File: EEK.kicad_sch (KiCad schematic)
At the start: 34 parts

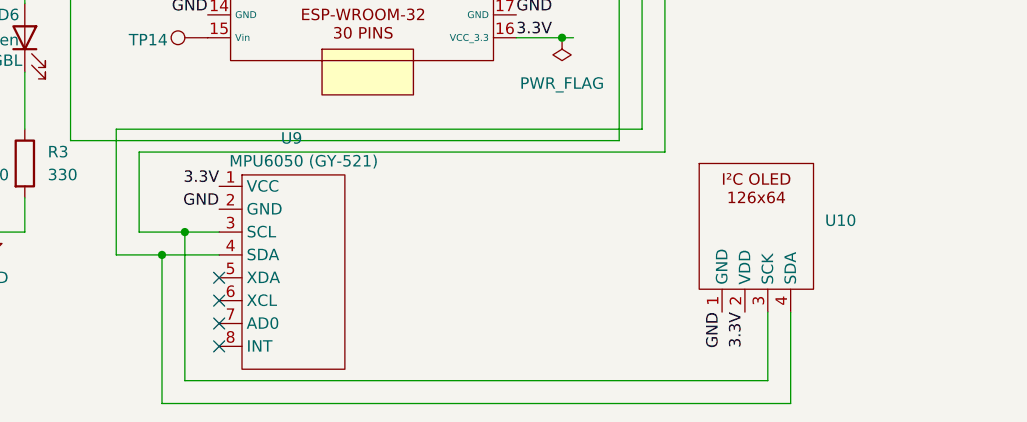
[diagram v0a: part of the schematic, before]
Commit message: fix the bug on OLED power supply pin1 and 2 inverted (3.3V and GND)
Fix the bug on the OLED power supply pins which have been inverted PIN 1 3.3V and pin 2 GND
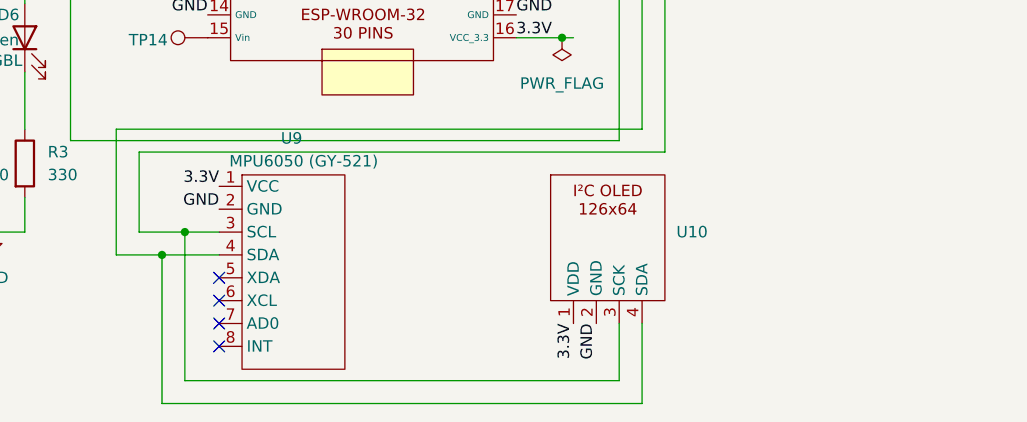
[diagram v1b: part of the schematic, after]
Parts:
- U10: footprint Connector_PinHeader_2.54mm:PinHeader_1x04_P2.54mm_Vertical -> (none)
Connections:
- net 3.3V: now also U10.1 (VDD); no longer U10.2 (VDD)
- net GND: now also U10.2 (GND); no longer U10.1 (GND)
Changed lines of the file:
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@@
+	(wire
+		(pts
+			(xy 127 124.46) (xy 73.66 124.46)
+		)
+		(stroke
+			(width 0)
+			(type default)
+		)
+	)
 	(wire
 		(pts
@@
 	(wire
 		(pts
+			(xy 124.46 121.92) (xy 76.2 121.92)
+		)
+		(stroke
+			(width 0)
+			(type default)
+		)
+	)
+	(wire
+		(pts
 			(xy 127 58.42) (xy 127 93.98)
 		)
@@
 	(wire
 		(pts
-			(xy 143.51 124.46) (xy 73.66 124.46)
-		)
-		(stroke
-			(width 0)
-			(type default)
-		)
-	)
-	(wire
-		(pts
 			(xy 73.66 107.95) (xy 80.01 107.95)
 		)
@@
 	(wire
 		(pts
-			(xy 140.97 114.3) (xy 140.97 121.92)
-		)
-		(stroke
-			(width 0)
-			(type default)
-		)
-	)
-	(wire
-		(pts
 			(xy 66.04 43.18) (xy 41.91 43.18)
 		)
@@
 	(wire
 		(pts
+			(xy 124.46 115.57) (xy 124.46 121.92)
+		)
+		(stroke
+			(width 0)
+			(type default)
+		)
+	)
+	(wire
+		(pts
 			(xy 60.96 68.58) (xy 78.74 68.58)
 		)
@@
 	(wire
 		(pts
-			(xy 143.51 114.3) (xy 143.51 124.46)
-		)
-		(stroke
-			(width 0)
-			(type default)
-		)
-	)
-	(wire
-		(pts
 			(xy 41.91 64.77) (xy 49.53 64.77)
 		)
@@
 	(wire
 		(pts
-			(xy 140.97 121.92) (xy 76.2 121.92)
-		)
-		(stroke
-			(width 0)
-			(type default)
-		)
-	)
-	(wire
-		(pts
 			(xy 68.58 71.12) (xy 78.74 71.12)
 		)
@@
 		(pts
 			(xy 77.47 60.96) (xy 78.74 60.96)
+		)
+		(stroke
+			(width 0)
+			(type default)
+		)
+	)
+	(wire
+		(pts
+			(xy 127 115.57) (xy 127 124.46)
 		)
 		(stroke
@@
 	)
 	(label "3.3V"
-		(at 138.43 114.3 270)
+		(at 119.38 115.57 270)
 		(fields_autoplaced yes)
 		(effects
@@
 	)
 	(label "GND"
-		(at 135.89 114.3 270)
+		(at 121.92 115.57 270)
 		(fields_autoplaced yes)
 		(effects
@@
 				(path "/0a4f8f30-fcea-49ae-bc76-20e4ae5d80ad"
 					(reference "TP4")
+					(unit 1)
+				)
+			)
+		)
+	)
+	(symbol
+		(lib_name "126x64_I²C_OLED_1")
+		(lib_id "PH_LIB_sym:126x64_I²C_OLED")
+		(at 118.11 101.6 0)
+		(unit 1)
+		(exclude_from_sim no)
+		(in_bom yes)
+		(on_board yes)
+		(dnp no)
+		(fields_autoplaced yes)
+		(property "Reference" "U10"
+			(at 130.81 105.4099 0)
+			(effects
+				(font
+					(size 1.27 1.27)
+				)
+				(justify left)
+			)
+		)
+		(property "Value" "~"
+			(at 130.81 107.315 0)
+			(effects
+				(font
+					(size 1.27 1.27)
+				)
+				(justify left)
+			)
+		)
+		(property "Footprint" ""
+			(at 118.11 101.6 0)
+			(effects
+				(font
+					(size 1.27 1.27)
+				)
+				(hide yes)
+			)
+		)
+		(property "Datasheet" ""
+			(at 118.11 101.6 0)
+			(effects
+				(font
+					(size 1.27 1.27)
+				)
+				(hide yes)
+			)
+		)
+		(property "Description" ""
+			(at 118.11 101.6 0)
+			(effects
+				(font
+					(size 1.27 1.27)
+				)
+				(hide yes)
+			)
+		)
+		(pin "3"
+		)
+		(pin "2"
+		)
+		(pin "4"
+		)
+		(pin "1"
+		)
+		(instances
+			(project "EEK"
+				(path "/0a4f8f30-fcea-49ae-bc76-20e4ae5d80ad"
+					(reference "U10")
 					(unit 1)
 				)
@@
 					(unit 1)
 				)
-			)
-		)
-	)
-	(symbol
-		(lib_id "PH_LIB_sym:126x64_I²C_OLED")
-		(at 134.62 100.33 0)
-		(unit 1)
-		(exclude_from_sim no)
-		(in_bom yes)
-		(on_board yes)
-		(dnp no)
-		(fields_autoplaced yes)
-		(property "Reference" "U10"
-			(at 147.32 104.1399 0)
-			(effects
-				(font
-					(size 1.27 1.27)
-				)
-				(justify left)
-			)
-		)
-		(property "Value" "~"
-			(at 147.32 106.045 0)
-			(effects
-				(font
-					(size 1.27 1.27)
-				)
-				(justify left)
-			)
-		)
-		(property "Footprint" "Connector_PinHeader_2.54mm:PinHeader_1x04_P2.54mm_Vertical"
-			(at 134.62 100.33 0)
-			(effects
-				(font
-					(size 1.27 1.27)
-				)
-				(hide yes)
-			)
-		)
-		(property "Datasheet" ""
-			(at 134.62 100.33 0)
-			(effects
-				(font
-					(size 1.27 1.27)
-				)
-				(hide yes)
-			)
-		)
-		(property "Description" ""
-			(at 134.62 100.33 0)
-			(effects
-				(font
-					(size 1.27 1.27)
-				)
-				(hide yes)
-			)
-		)
-		(pin "2"
-		)
-		(pin "3"
-		)
-		(pin "4"
-		)
-		(pin "1"
-		)
-		(instances
-			(project "EEK"
-				(path "/0a4f8f30-fcea-49ae-bc76-20e4ae5d80ad"
-					(reference "U10")
-					(unit 1)
-				)

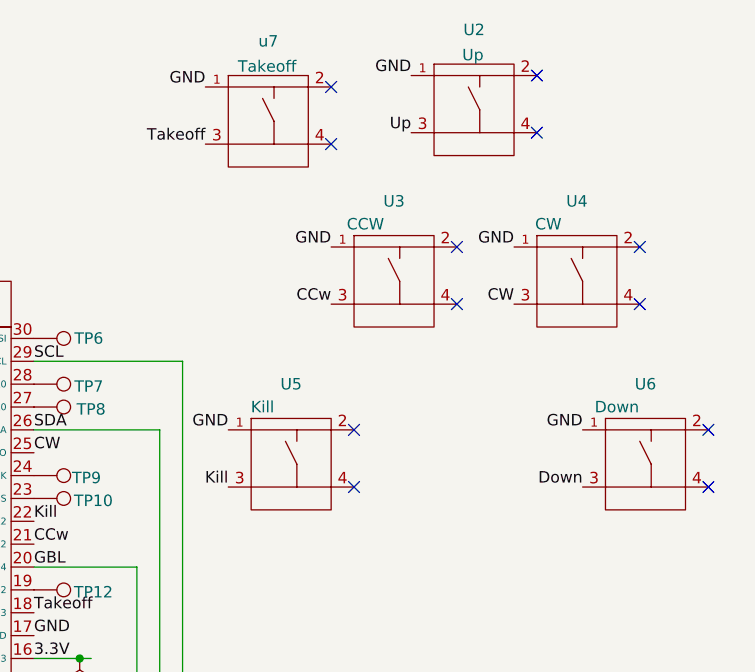
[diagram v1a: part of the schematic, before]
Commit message: change the footprint of the tactil switch which was not correct
Change the footprint of the tactil switch which was not correct
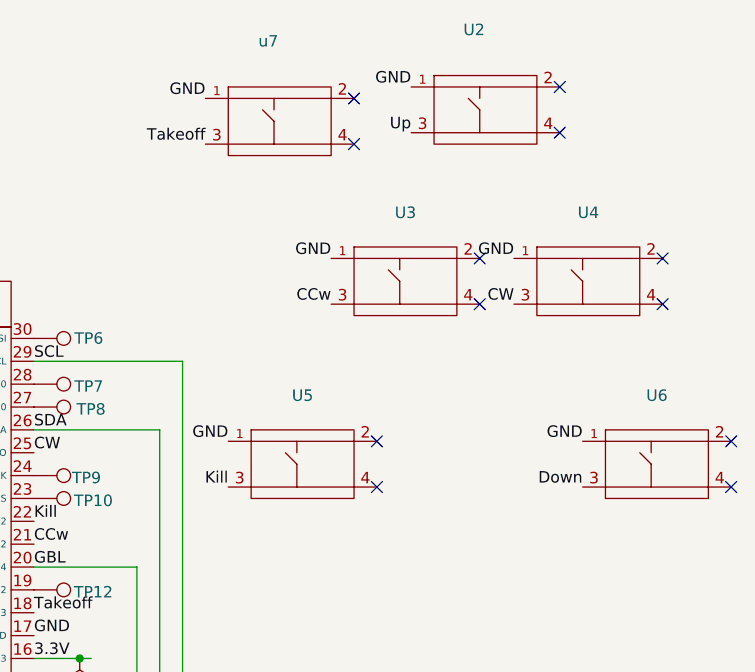
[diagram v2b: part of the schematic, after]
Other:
- moved on the sheet: U2, U3, U4, U5, U6, u7
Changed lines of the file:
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@@
 	)
 	(no_connect
-		(at 148.59 64.77)
+		(at 151.13 64.77)
 	)
 	(no_connect
-		(at 180.34 38.1)
+		(at 182.88 39.37)
 	)
 	(no_connect
-		(at 180.34 44.45)
+		(at 182.88 44.45)
 	)
 	(no_connect
@@
 	)
 	(no_connect
-		(at 168.91 19.05)
+		(at 171.45 20.32)
 	)
 	(no_connect
-		(at 187.96 58.42)
+		(at 190.5 59.69)
 	)
 	(no_connect
@@
 	)
 	(no_connect
-		(at 187.96 64.77)
+		(at 190.5 64.77)
 	)
 	(no_connect
-		(at 146.05 26.67)
+		(at 148.59 26.67)
 	)
 	(no_connect
-		(at 160.02 38.1)
+		(at 162.56 39.37)
 	)
 	(no_connect
@@
 	)
 	(no_connect
-		(at 148.59 58.42)
+		(at 151.13 59.69)
 	)
 	(no_connect
-		(at 160.02 44.45)
+		(at 162.56 44.45)
 	)
 	(no_connect
-		(at 168.91 25.4)
+		(at 171.45 25.4)
 	)
 	(no_connect
-		(at 146.05 20.32)
+		(at 148.59 21.59)
 	)
 	(wire
@@
 	)
 	(label "GND"
-		(at 154.94 19.05 180)
+		(at 154.94 20.32 180)
 		(fields_autoplaced yes)
 		(effects
@@
 	)
 	(label "GND"
-		(at 132.08 20.32 180)
+		(at 132.08 21.59 180)
 		(fields_autoplaced yes)
 		(effects
@@
 		)
 		(property "Netclass" "GND"
-			(at 132.08 21.59 0)
+			(at 132.08 22.86 0)
 			(effects
 				(font
@@
 	)
 	(label "GND"
-		(at 146.05 38.1 180)
+		(at 146.05 39.37 180)
 		(fields_autoplaced yes)
 		(effects
@@
 	)
 	(label "GND"
-		(at 166.37 38.1 180)
+		(at 166.37 39.37 180)
 		(fields_autoplaced yes)
 		(effects
@@
 	)
 	(label "GND"
-		(at 173.99 58.42 180)
+		(at 173.99 59.69 180)
 		(fields_autoplaced yes)
 		(effects
@@
 	)
 	(label "GND"
-		(at 134.62 58.42 180)
+		(at 134.62 59.69 180)
 		(fields_autoplaced yes)
 		(effects
@@
 	)
 	(symbol
-		(lib_name "SW_tactile_1")
 		(lib_id "PH_LIB_sym:SW_tactile")
 		(at 135.89 17.78 0)
@@
 		)
 		(property "Description" "Takeoff"
-			(at 138.938 18.034 0)
+			(at 135.89 17.78 0)
 			(effects
 				(font
 					(size 1.27 1.27)
 				)
+				(hide yes)
 			)
 		)
@@
 	)
 	(symbol
-		(lib_name "SW_tactile_1")
 		(lib_id "PH_LIB_sym:SW_tactile")
 		(at 158.75 16.51 0)
@@
 		)
 		(property "Description" "Up"
-			(at 161.798 16.764 0)
+			(at 158.75 16.51 0)
 			(effects
 				(font
 					(size 1.27 1.27)
 				)
+				(hide yes)
 			)
 		)
@@
 	)
 	(symbol
-		(lib_name "SW_tactile_1")
 		(lib_id "PH_LIB_sym:SW_tactile")
 		(at 149.86 35.56 0)
@@
 		(fields_autoplaced yes)
 		(property "Reference" "U3"
-			(at 153.035 33.02 0)
+			(at 154.305 34.29 0)
 			(effects
 				(font
@@
 		)
 		(property "Value" "~"
-			(at 153.035 35.56 0)
+			(at 154.305 36.83 0)
 			(effects
 				(font
@@
 					(size 1.27 1.27)
 				)
+				(hide yes)
 			)
 		)
@@
 	)
 	(symbol
-		(lib_name "SW_tactile_1")
 		(lib_id "PH_LIB_sym:SW_tactile")
 		(at 138.43 55.88 0)
@@
 		(fields_autoplaced yes)
 		(property "Reference" "U5"
-			(at 141.605 53.34 0)
+			(at 142.875 54.61 0)
 			(effects
 				(font
@@
 		)
 		(property "Value" "~"
-			(at 141.605 55.88 0)
+			(at 142.875 57.15 0)
 			(effects
 				(font
@@
 					(size 1.27 1.27)
 				)
+				(hide yes)
 			)
 		)
@@
 	)
 	(symbol
-		(lib_name "SW_tactile_1")
 		(lib_id "PH_LIB_sym:SW_tactile")
 		(at 170.18 35.56 0)
@@
 		(fields_autoplaced yes)
 		(property "Reference" "U4"
-			(at 173.355 33.02 0)
+			(at 174.625 34.29 0)
 			(effects
 				(font
@@
 		)
 		(property "Value" "~"
-			(at 173.355 35.56 0)
+			(at 174.625 36.83 0)
 			(effects
 				(font
@@
 					(size 1.27 1.27)
 				)
+				(hide yes)
 			)
 		)
@@
 	)
 	(symbol
-		(lib_name "SW_tactile_1")
 		(lib_id "PH_LIB_sym:SW_tactile")
 		(at 177.8 55.88 0)
@@
 		(fields_autoplaced yes)
 		(property "Reference" "U6"
-			(at 180.975 53.34 0)
+			(at 182.245 54.61 0)
 			(effects
 				(font
@@
 		)
 		(property "Value" "~"
-			(at 180.975 55.88 0)
+			(at 182.245 57.15 0)
 			(effects
 				(font
@@
 					(size 1.27 1.27)
 				)
+				(hide yes)
 			)
 		)

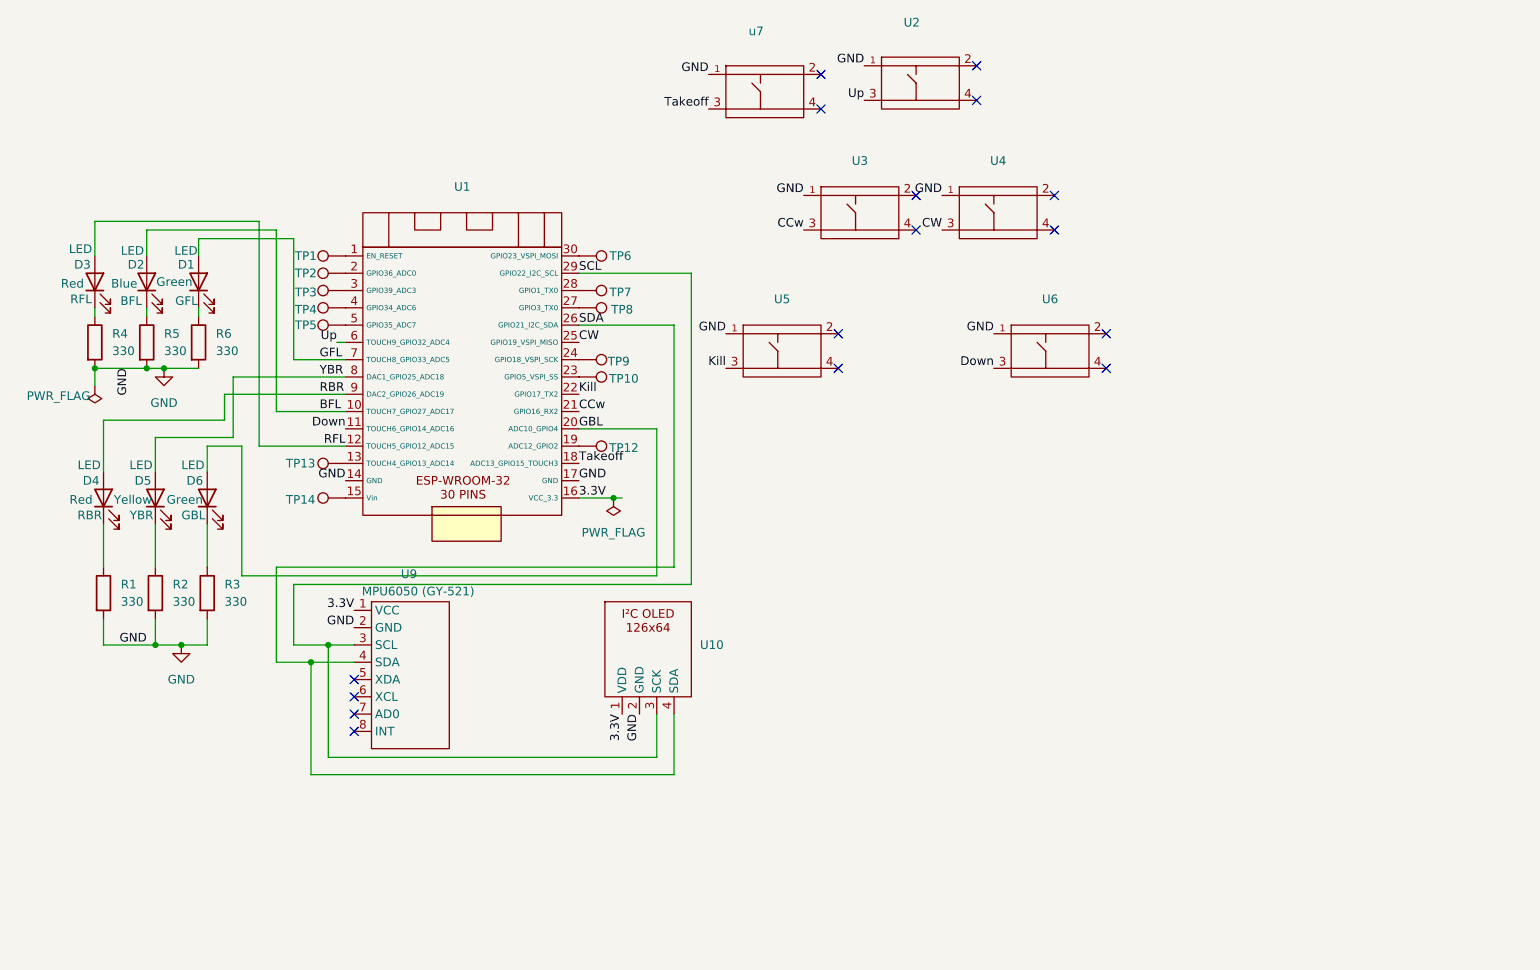
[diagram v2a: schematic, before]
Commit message: Addvcapacitors for the switches and connector for battery
Add capacitors for the switches and connector for battery Vin
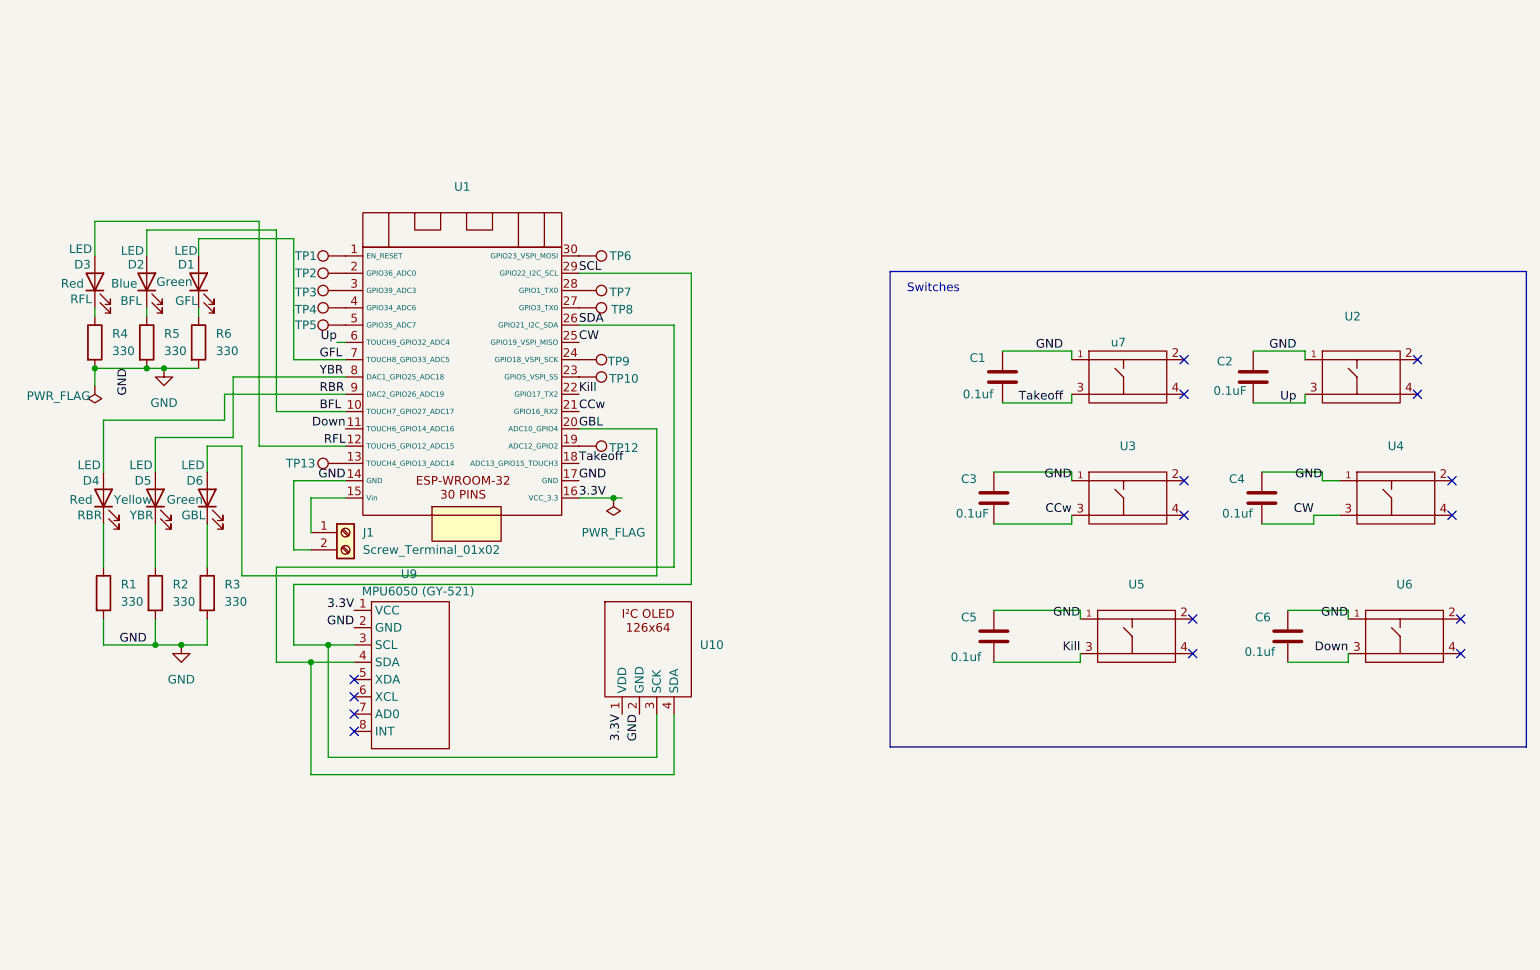
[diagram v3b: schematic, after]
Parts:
- removed TP14: TestPoint, TestPoint:TestPoint_Plated_Hole_D2.0mm, symbol Connector:TestPoint
- added C1, C4, C5, C6: 0.1uf, Capacitor_THT:C_Disc_D8.0mm_W2.5mm_P5.00mm, symbol Device:C
- added C2, C3: 0.1uF, Capacitor_THT:C_Disc_D8.0mm_W2.5mm_P5.00mm, symbol Device:C
- added J1: Screw_Terminal_01x02, TerminalBlock_Phoenix:TerminalBlock_Phoenix_MKDS-1,5-2_1x02_P5.00mm_Horizontal, symbol Connector:Screw_Terminal_01x02
- U10: footprint (none) -> TerminalBlock_Phoenix:TerminalBlock_Phoenix_MKDS-1,5-4_1x04_P5.00mm_Horizontal
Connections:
- net CCw: now also C3.2
- net CW: now also C4.2
- net Down: now also C6.2
- net GND: now also C1.1, C2.1, C3.1, C4.1, C5.1, C6.1, J1.2 (Pin_2)
- net Kill: now also C5.2
- net Takeoff: now also C1.2
- net Up: now also C2.2
- net at U1.15 (Vin): now also J1.1 (Pin_1)
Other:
- note added: "Switches"
- moved on the sheet: U2, U3, U4, U5, U6, u7
